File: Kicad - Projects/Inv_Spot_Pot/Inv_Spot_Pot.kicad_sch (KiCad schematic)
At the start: 24 parts, among them J1 Screw_Terminal_01x03, J2 PWM, J3 Power_Supply, J4 Current_Sense, J5 Temperature_Sense, Q1 40T120, Q2 40T120, T1 Transformer_1P_2S, U1 IR2110

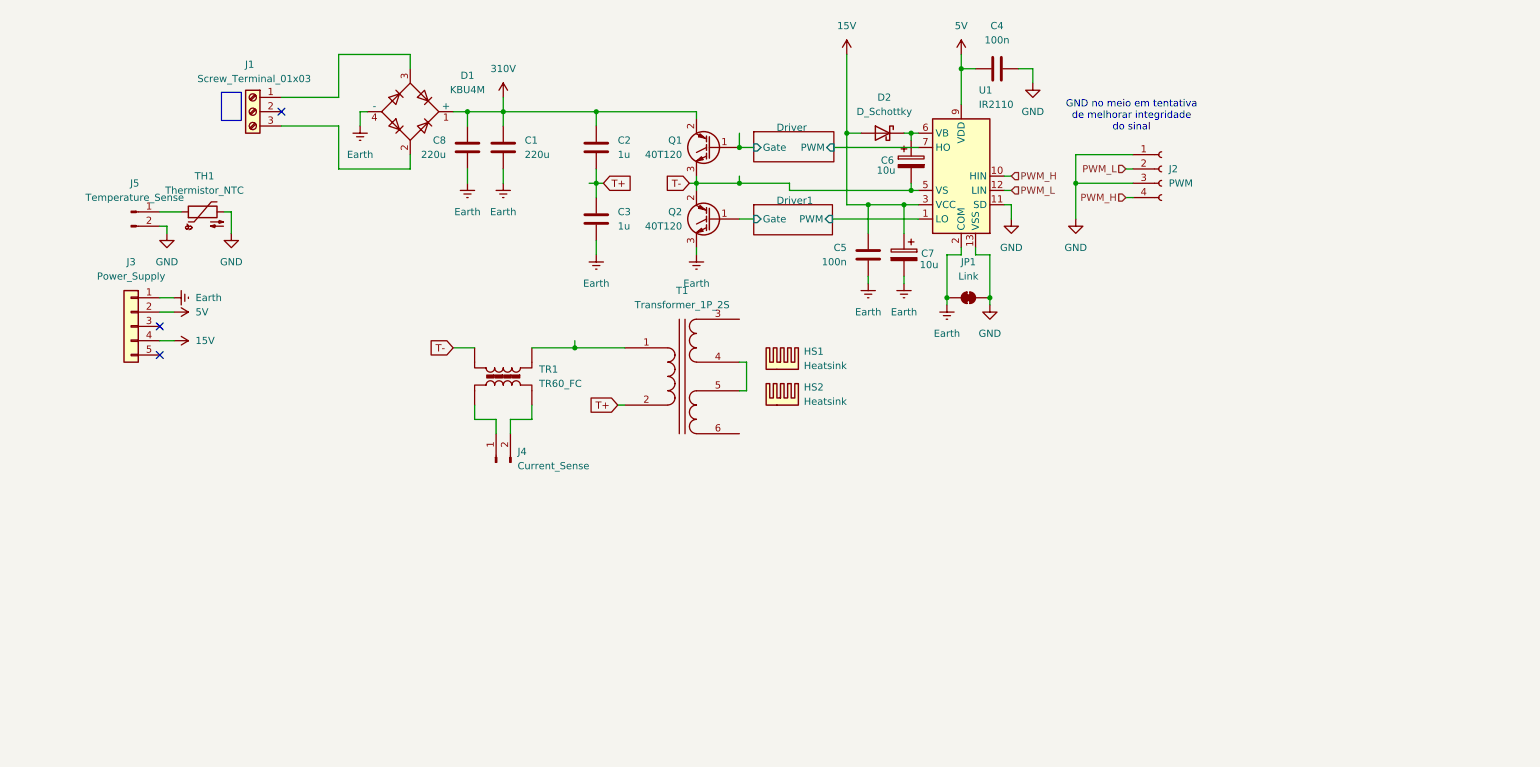
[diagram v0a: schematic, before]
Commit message: Updated PCB
Fixed some footprints, increased insulation and improved board segmentation - segmentation still needs some work
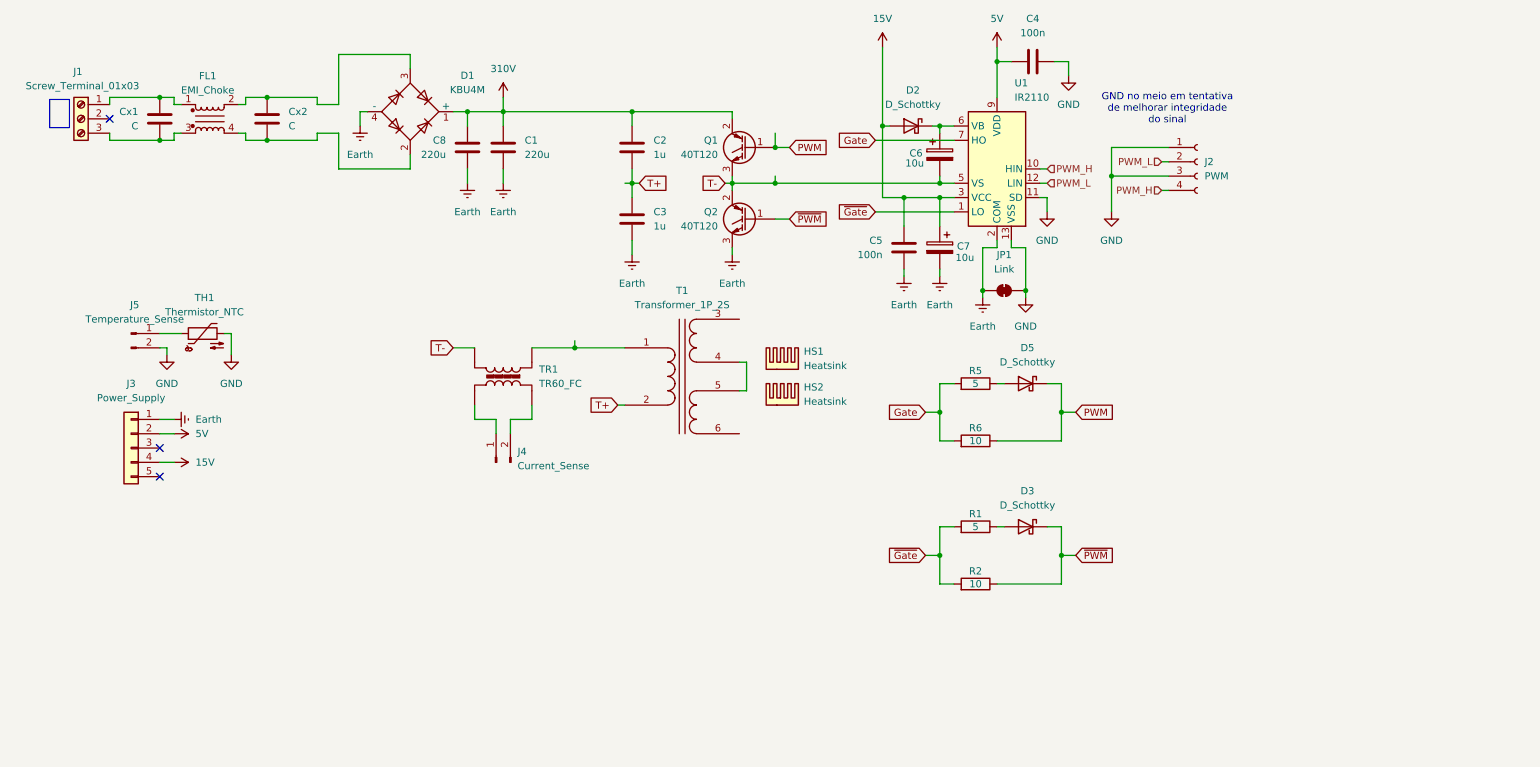
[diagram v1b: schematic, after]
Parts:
- added Cx1, Cx2: C, Capacitor_THT:C_Rect_L24.0mm_W8.6mm_P22.50mm_MKT, symbol Device:C
- added D3, D5: D_Schottky, Diode_SMD:D_SOD-123F, symbol Device:D_Schottky
- added FL1: EMI_Choke, Inductor_THT:Filtro_Choke, symbol Filter:Choke_Schaffner_RN102-0.3-02-12M
- added R1, R5: 5, Resistor_SMD:R_1206_3216Metric_Pad1.30x1.75mm_HandSolder, symbol Device:R
- added R2, R6: 10, Resistor_SMD:R_1206_3216Metric_Pad1.30x1.75mm_HandSolder, symbol Device:R
- D2: footprint Diode_SMD:D_SOD-123F -> Diode_SMD:D_SMA
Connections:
- net at D1.2: now also Cx2.2, FL1.4; no longer J1.3 (Pin_3)
- net at D1.3: now also Cx2.1, FL1.2; no longer J1.1 (Pin_1)
- net Driver/Gate renamed PWM
- net PWM: now also D5.1 (K), R6.1
- net Driver/PWM renamed Gate
- net Gate: now also R5.2, R6.2
- net Driver1/Gate renamed ~{PWM}
- net ~{PWM}: now also D3.1 (K), R2.1
- net Driver1/PWM renamed ~{Gate}
- net ~{Gate}: now also R1.2, R2.2
- new net: D3.2 (A), R1.1
- new net: Cx1.1, FL1.1, J1.1 (Pin_1)
- new net: Cx1.2, FL1.3, J1.3 (Pin_3)
- new net: D5.2 (A), R5.1
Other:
- removed sheet Driver
- removed sheet Driver1
- moved on the sheet: C2, C3, C4, C5, C6, C7, D2, J1, J2, J3, J5, JP1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

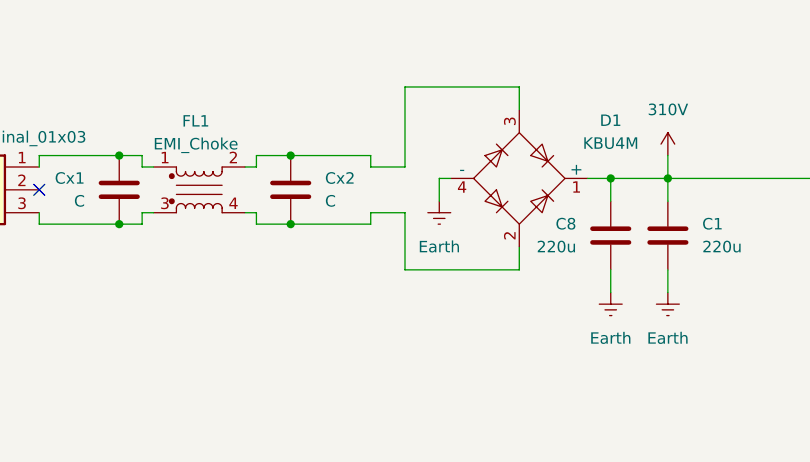
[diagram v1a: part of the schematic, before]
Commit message: Final revision for board with driver IC
Última revisão da placa com driver IR2110 - para melhor flexibilidade e aproveitamento de espaço da placa, foi decidido explorar o projeto com um transformador de gate drive EE-25

Poderia ser utilizado um transformador EE-19 e poupar espaço, mas por disponibilidade imediata foi utilizado o EEL-25
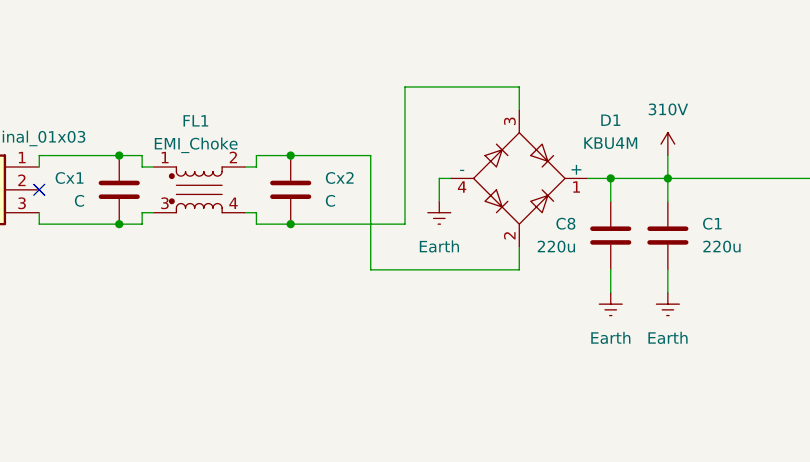
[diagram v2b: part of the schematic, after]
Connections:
- net at Cx2.2, FL1.4: now also D1.3; no longer D1.2
- net at Cx2.1, FL1.2: now also D1.2; no longer D1.3
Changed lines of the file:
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@@
 	(wire
 		(pts
-			(xy 57.15 73.66) (xy 66.04 73.66)
+			(xy 57.15 73.66) (xy 69.85 73.66)
 		)
 		(stroke
@@
 	(wire
 		(pts
-			(xy 69.85 72.39) (xy 69.85 78.74)
-		)
-		(stroke
-			(width 0)
-			(type default)
-		)
-	)
-	(wire
-		(pts
 			(xy 170.18 83.82) (xy 166.37 83.82)
 		)
@@
 	(wire
 		(pts
-			(xy 69.85 78.74) (xy 82.55 78.74)
-		)
-		(stroke
-			(width 0)
-			(type default)
-		)
-	)
-	(wire
-		(pts
 			(xy 82.55 58.42) (xy 82.55 60.96)
 		)
@@
 	(wire
 		(pts
+			(xy 66.04 66.04) (xy 66.04 78.74)
+		)
+		(stroke
+			(width 0)
+			(type default)
+		)
+	)
+	(wire
+		(pts
 			(xy 198.12 121.92) (xy 198.12 127)
 		)
@@
 	(wire
 		(pts
+			(xy 66.04 78.74) (xy 82.55 78.74)
+		)
+		(stroke
+			(width 0)
+			(type default)
+		)
+	)
+	(wire
+		(pts
 			(xy 138.43 81.28) (xy 139.7 81.28)
 		)
@@
 	(wire
 		(pts
-			(xy 66.04 67.31) (xy 69.85 67.31)
-		)
-		(stroke
-			(width 0)
-			(type default)
-		)
-	)
-	(wire
-		(pts
 			(xy 215.9 82.55) (xy 217.17 82.55)
 		)
@@
 	(wire
 		(pts
-			(xy 66.04 66.04) (xy 66.04 67.31)
-		)
-		(stroke
-			(width 0)
-			(type default)
-		)
-	)
-	(wire
-		(pts
 			(xy 92.71 68.58) (xy 92.71 71.12)
 		)
@@
 	(wire
 		(pts
-			(xy 66.04 72.39) (xy 66.04 73.66)
-		)
-		(stroke
-			(width 0)
-			(type default)
-		)
-	)
-	(wire
-		(pts
 			(xy 147.32 80.01) (xy 147.32 81.28)
 		)
@@
 	(wire
 		(pts
-			(xy 69.85 67.31) (xy 69.85 58.42)
+			(xy 69.85 58.42) (xy 69.85 73.66)
 		)
 		(stroke
@@
 		)
 		(stroke
-			(width 0)
-			(type default)
-		)
-	)
-	(wire
-		(pts
-			(xy 69.85 72.39) (xy 66.04 72.39)
-		)
-		(stroke

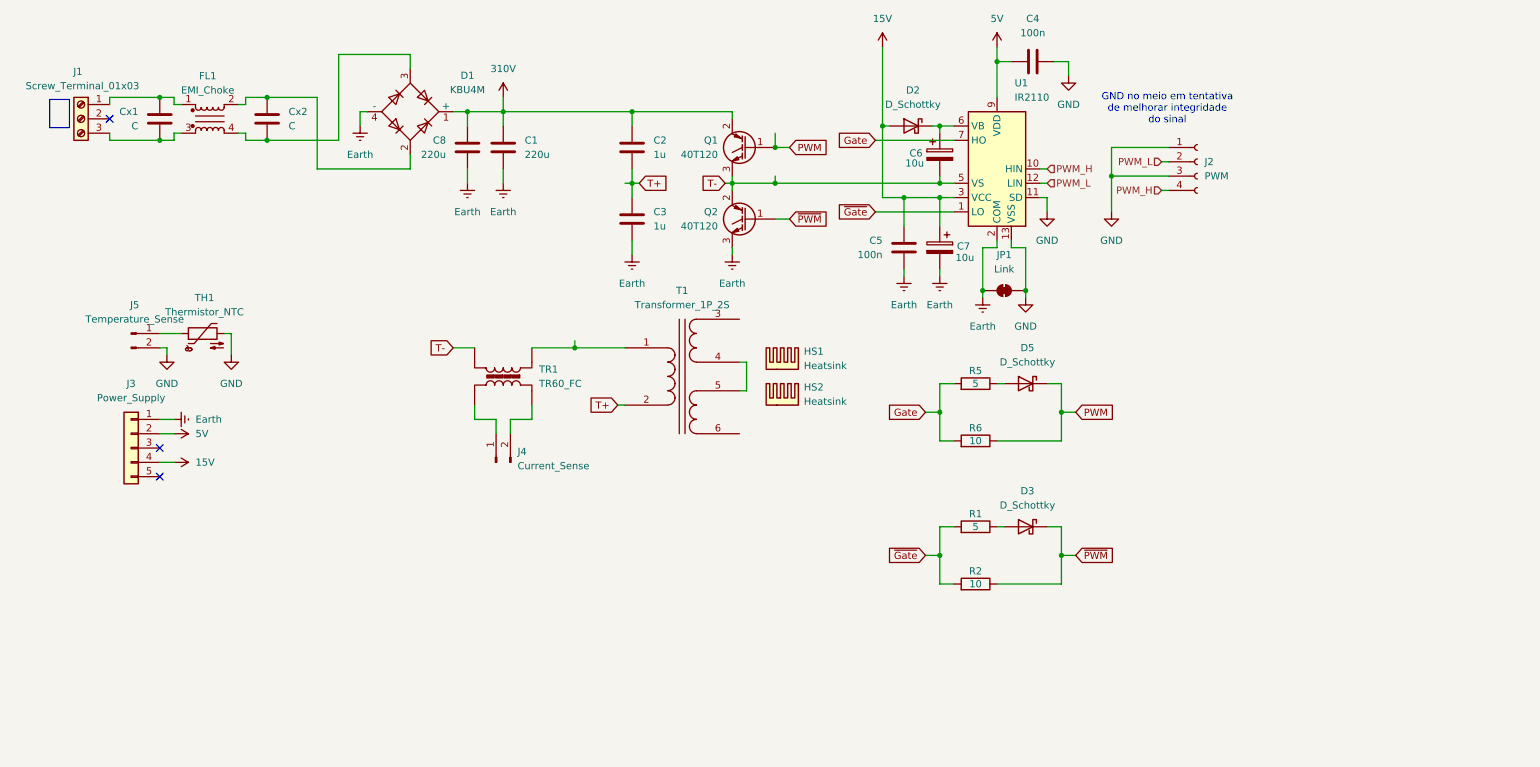
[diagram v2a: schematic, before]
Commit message: Half bridge prototype
IR2110 completamente substituído por transformador de gate, falta corrigir footprint do transformador de saída e fazer placa alternativa de ponte completa
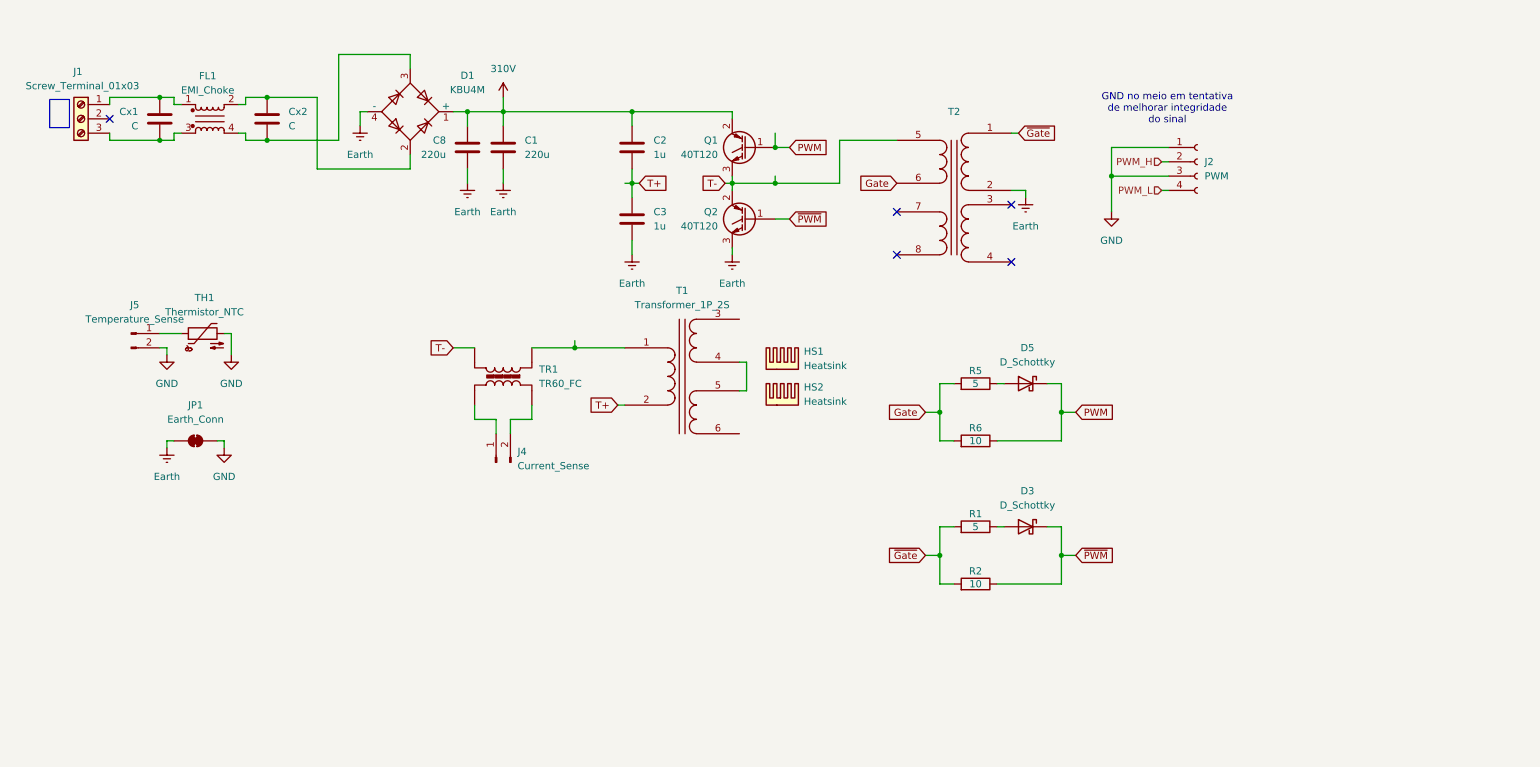
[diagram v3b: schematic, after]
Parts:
- removed C4, C5: 100n, Capacitor_SMD:C_1206_3216Metric_Pad1.33x1.80mm_HandSolder, symbol Device:C
- removed C6, C7: 10u, Capacitor_THT:CP_Radial_D8.0mm_P3.50mm, symbol Device:C_Polarized
- removed D2: D_Schottky, Diode_SMD:D_SMA, symbol Device:D_Schottky
- removed J3: Power_Supply, Connector_JST:JST_EH_B5B-EH-A_1x05_P2.50mm_Vertical, symbol Connector_Generic:Conn_01x05
- removed U1: IR2110, Package_DIP:DIP-14_W7.62mm_LongPads, symbol Driver_FET:IR2110
- added T2: ~, Transformer_THT:Pulse_Transformer-EEL-25_26x20-4_Windings, symbol Custom_Transformers:Pulse_Transformer-4_Windings
- JP1: value Link -> Earth_Conn
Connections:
- net Earth: now also T2.2
- net Gate: now also T2.6
- net PWM_H: now also J2.2 (Pin_2); no longer J2.4 (Pin_4)
- net PWM_L: now also J2.4 (Pin_4); no longer J2.2 (Pin_2)
- net T-: now also T2.5
- net ~{Gate}: now also T2.1
- no-connect marks 3 -> 5

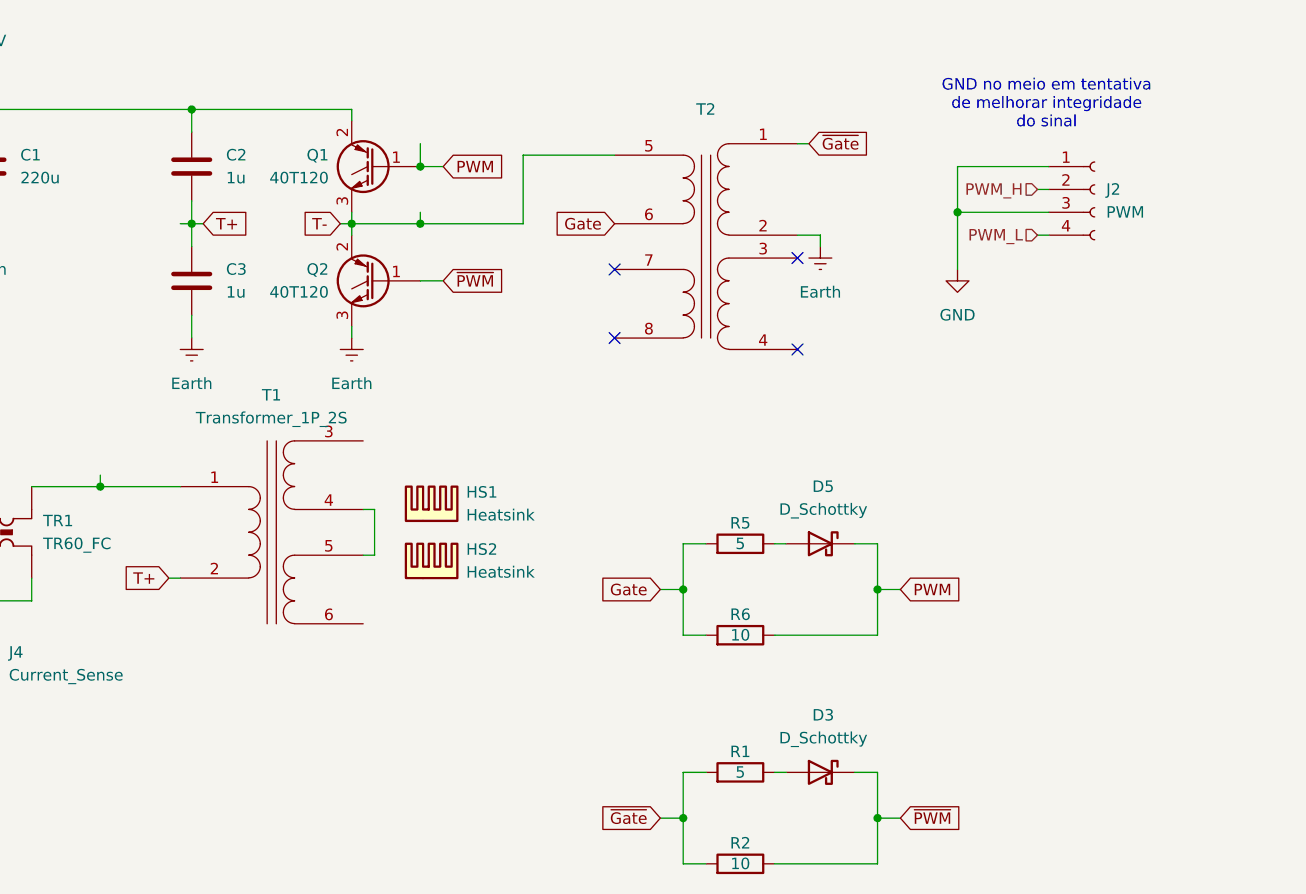
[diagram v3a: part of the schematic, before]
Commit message: Resistor CE
Adicionado resistor coletor-emissor na placa, corrigido erro na direção do diodo do circuito de drive dos IGBTs

Melhora nos planos de referência - Alguns pontos ainda apresentam caminho de retorno longos, mas talvez isso possa ser corrigido na própria placa
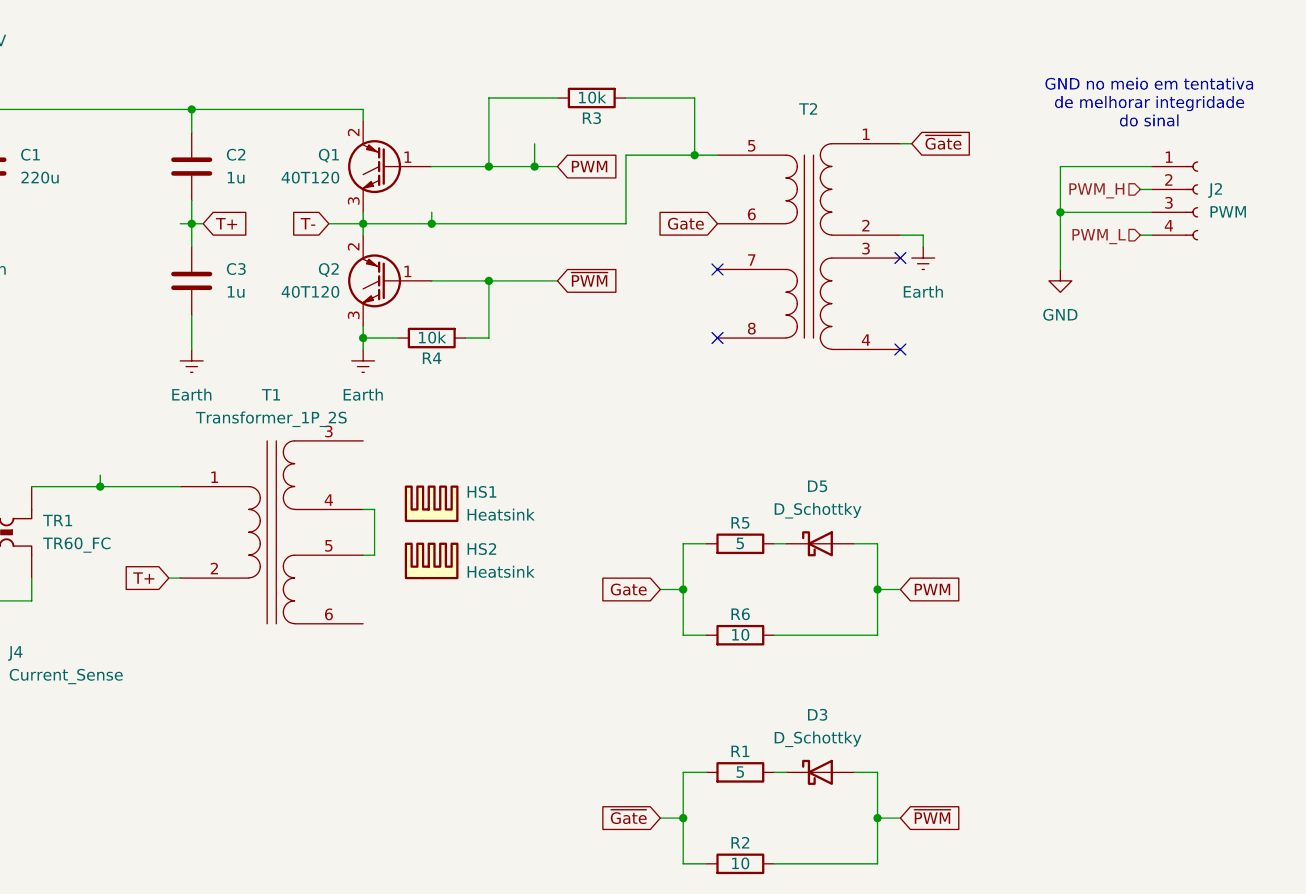
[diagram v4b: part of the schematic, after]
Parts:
- added R3, R4: 10k, Resistor_SMD:R_1206_3216Metric_Pad1.30x1.75mm_HandSolder, symbol Device:R
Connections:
- net Earth: now also R4.1
- net PWM: now also D5.2 (A), R3.1; no longer D5.1 (K)
- net T-: now also R3.2
- net ~{PWM}: now also D3.2 (A), R4.2; no longer D3.1 (K)
- net at R1.1: now also D3.1 (K); no longer D3.2 (A)
- net at R5.1: now also D5.1 (K); no longer D5.2 (A)
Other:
- moved on the sheet: J2, Q1, Q2, T2
